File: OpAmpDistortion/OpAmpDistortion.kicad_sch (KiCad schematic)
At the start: 20 parts, among them J1 INPUT, J2 OUTPUT, U1 NE5532

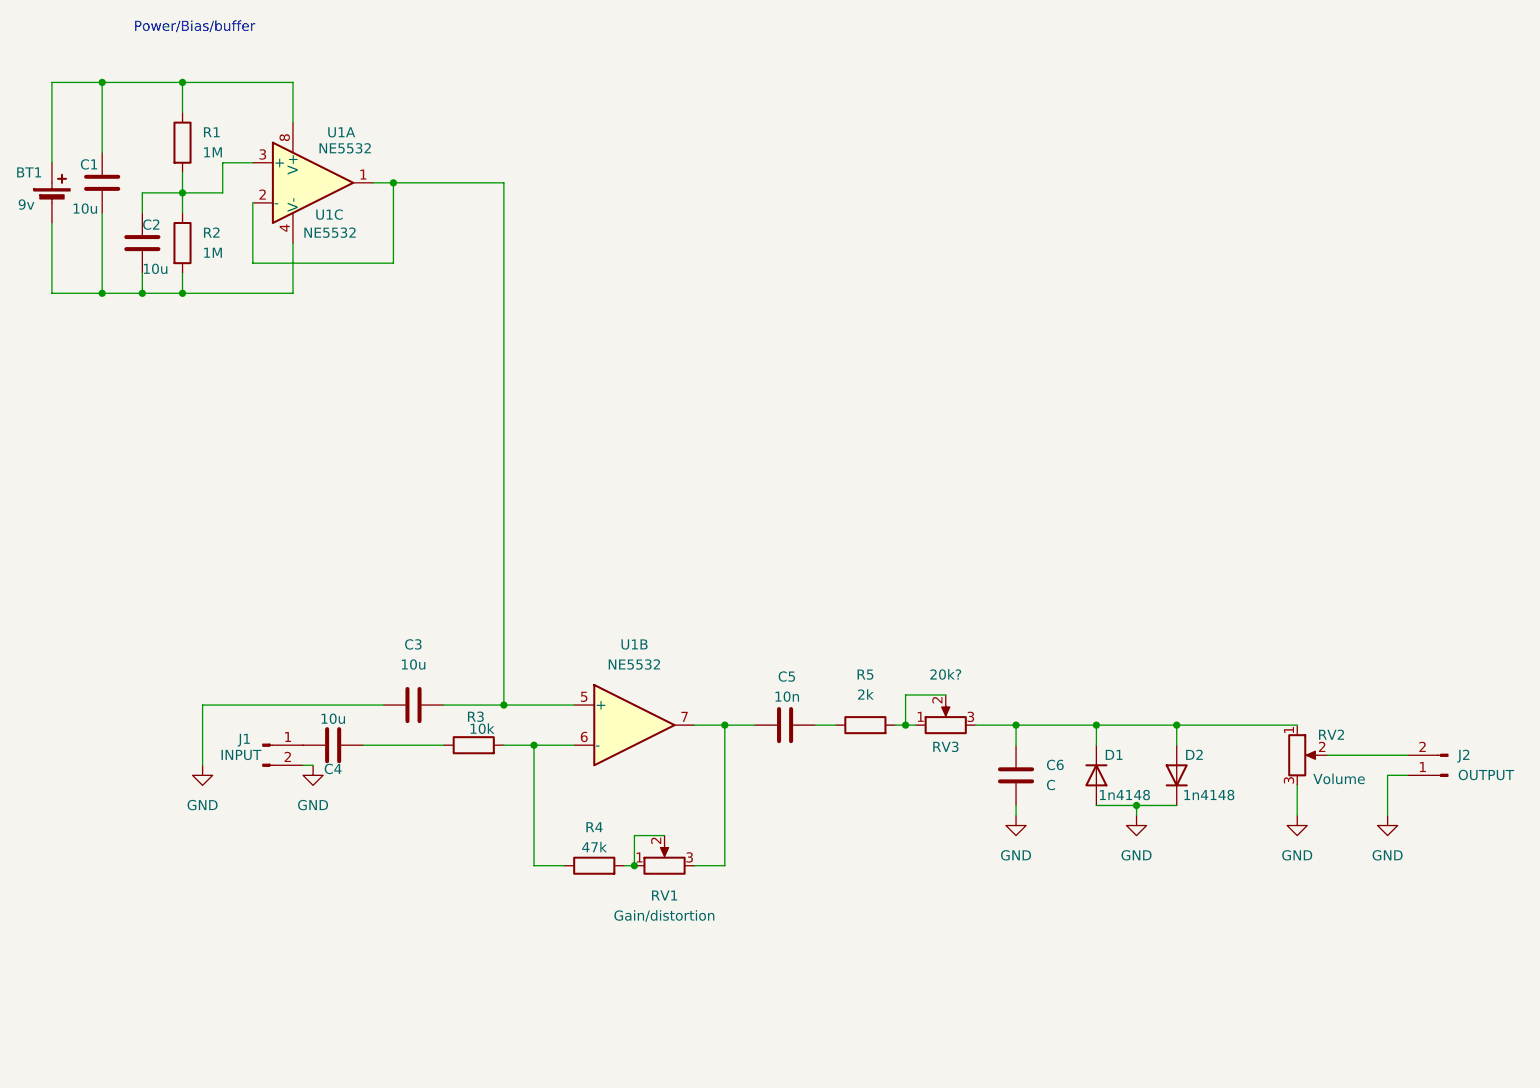
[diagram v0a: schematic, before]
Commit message: finished the first revision of the pcb schematic for op amp distortion
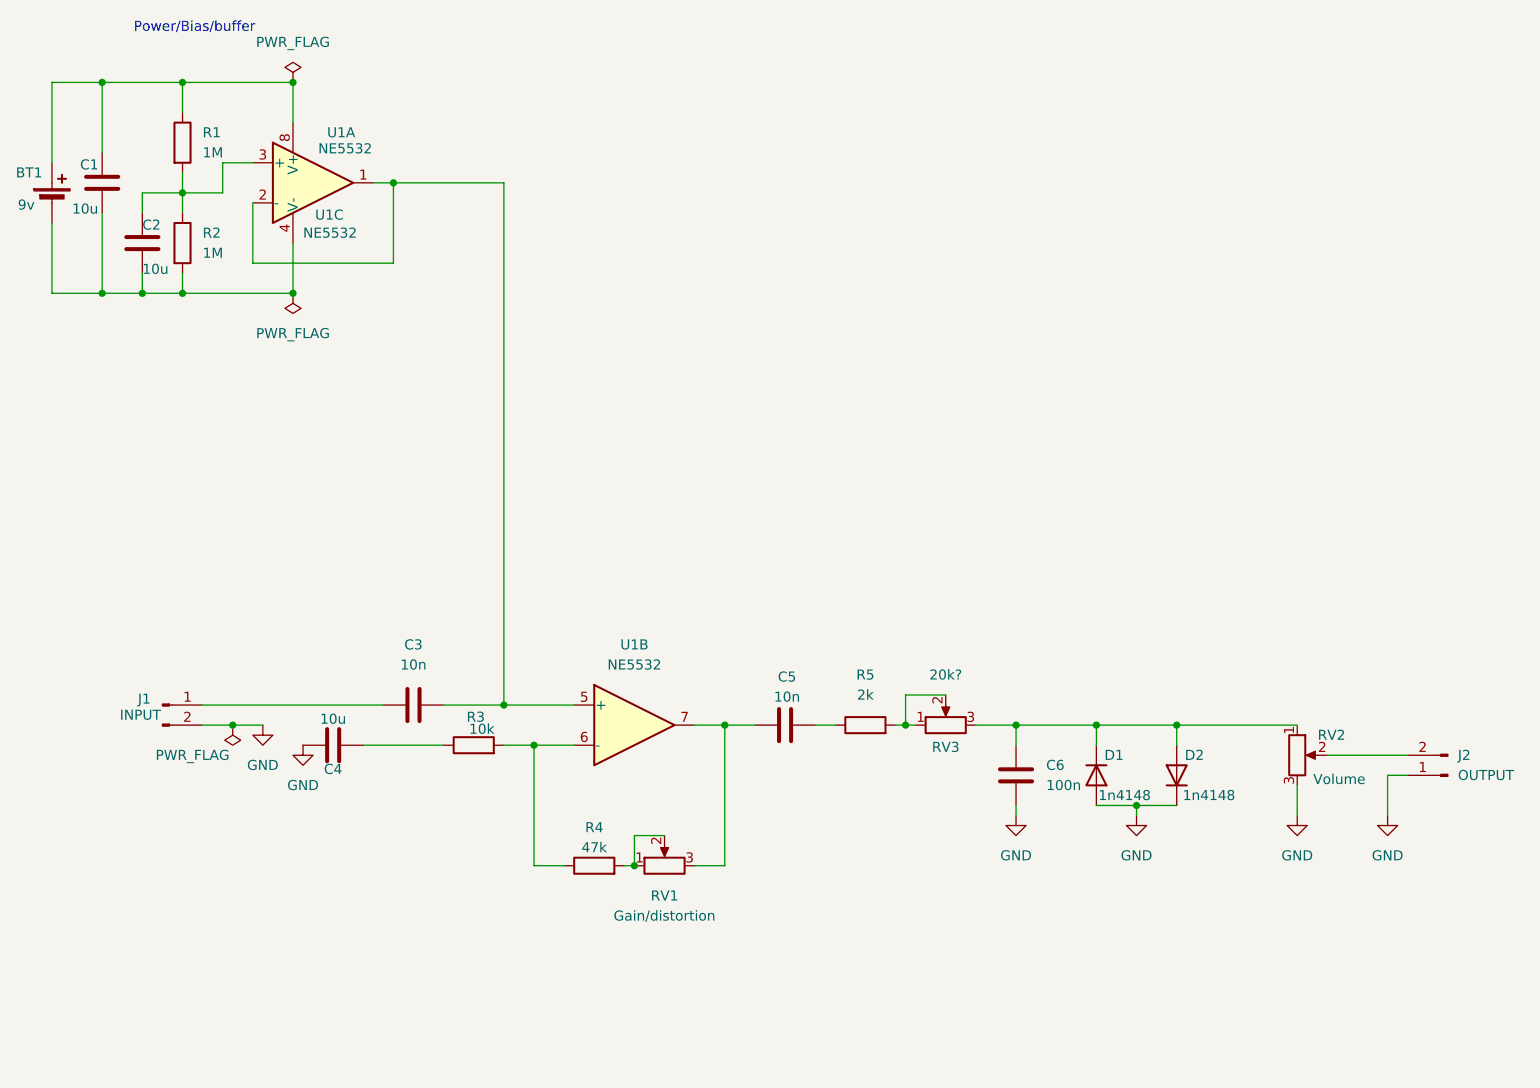
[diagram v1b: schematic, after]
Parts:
- C3: value 10u -> 10n
- C6: value C -> 100n
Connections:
- net GND: now also C4.1; no longer C3.1
- net at J1.1 (Pin_1): now also C3.1; no longer C4.1
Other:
- moved on the sheet: J1

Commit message: editied the PCB
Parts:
- added J3: Conn_01x02_Pin, symbol Connector:Conn_01x02_Pin
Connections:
- net GND: no longer J1.2 (Pin_2)
- net at C3.1: no longer J1.1 (Pin_1)
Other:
- moved on the sheet: BT1, C1, C2, J1, R1, R2, U1A, U1C

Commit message: added labeling to the pcb and made gerber 'wq
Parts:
- removed J3: Conn_01x02_Pin, symbol Connector:Conn_01x02_Pin
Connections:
- net GND: now also J1.2 (Pin_2)
- net at C3.1: now also J1.1 (Pin_1)
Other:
- moved on the sheet: J1
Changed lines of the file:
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@@
 		(lib_id "Connector:Conn_01x02_Pin")
 		(at 36.83 111.76 0)
-		(mirror y)
 		(unit 1)
 		(exclude_from_sim no)
@@
 		(dnp no)
 		(property "Reference" "J1"
-			(at 39.116 110.998 0)
+			(at 34.544 110.998 0)
 			(effects
 				(font
@@
 		)
 		(property "Value" "INPUT"
-			(at 39.624 113.03 0)
+			(at 34.036 113.03 0)
 			(effects
 				(font
@@
 					(unit 1)
 				)
-			)
-		)
-	)
-	(symbol
-		(lib_id "Connector:Conn_01x02_Pin")
-		(at 109.22 156.21 90)
-		(unit 1)
-		(exclude_from_sim no)
-		(in_bom yes)
-		(on_board yes)
-		(dnp no)
-		(fields_autoplaced yes)
-		(property "Reference" "J3"
-			(at 113.03 154.3049 90)
-			(effects
-				(font
-					(size 1.27 1.27)
-				)
-				(justify right)
-			)
-		)
-		(property "Value" "Conn_01x02_Pin"
-			(at 113.03 156.8449 90)
-			(effects
-				(font
-					(size 1.27 1.27)
-				)
-				(justify right)
-			)
-		)
-		(property "Footprint" ""
-			(at 109.22 156.21 0)
-			(effects
-				(font
-					(size 1.27 1.27)
-				)
-				(hide yes)
-			)
-		)
-		(property "Datasheet" "~"
-			(at 109.22 156.21 0)
-			(effects
-				(font
-					(size 1.27 1.27)
-				)
-				(hide yes)
-			)
-		)
-		(property "Description" "Generic connector, single row, 01x02, script generated"
-			(at 109.22 156.21 0)
-			(effects
-				(font
-					(size 1.27 1.27)
-				)
-				(hide yes)
-			)
-		)
-		(pin "2"
-		)
-		(pin "1"
-		)
-		(instances
-			(project ""
-				(path "/63e2fb5d-8ac3-4578-a4a1-86700891658c"
-					(reference "J3")
-					(unit 1)
-				)
